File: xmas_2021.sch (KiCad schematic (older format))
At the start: 45 parts, among them J1 SWIM, Q1 MMBT3904, SW1 User, U1 STM8L101F2P3

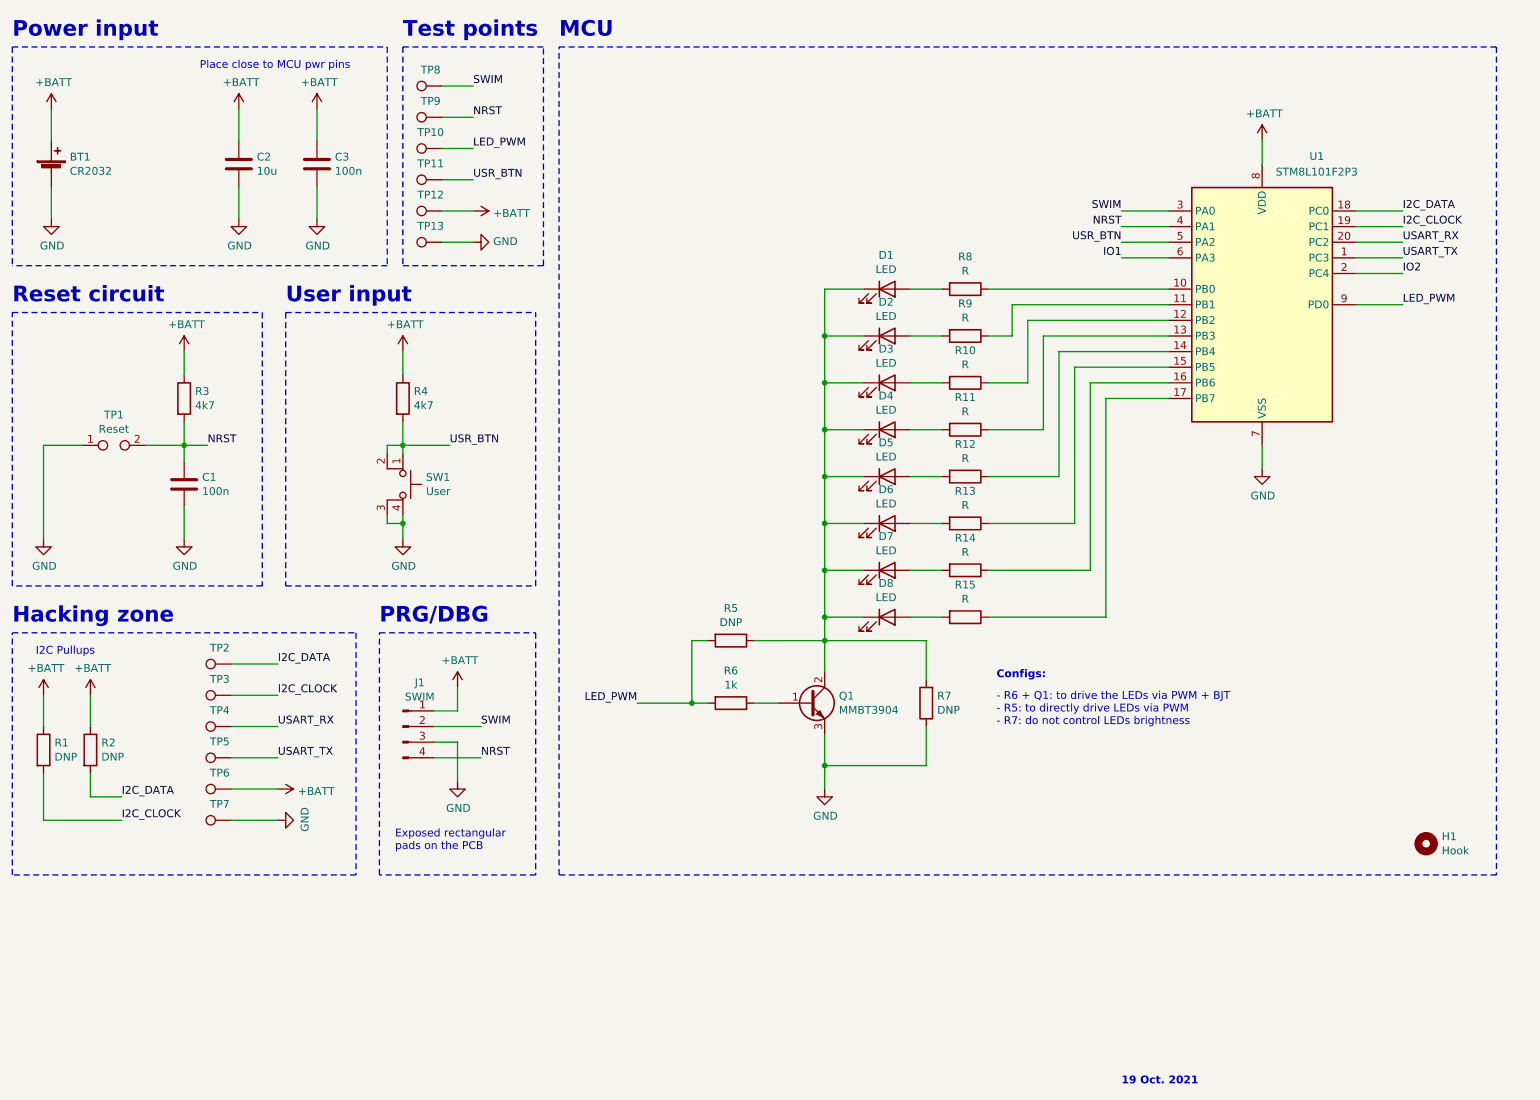
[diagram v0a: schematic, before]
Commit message: sch: update after hw test
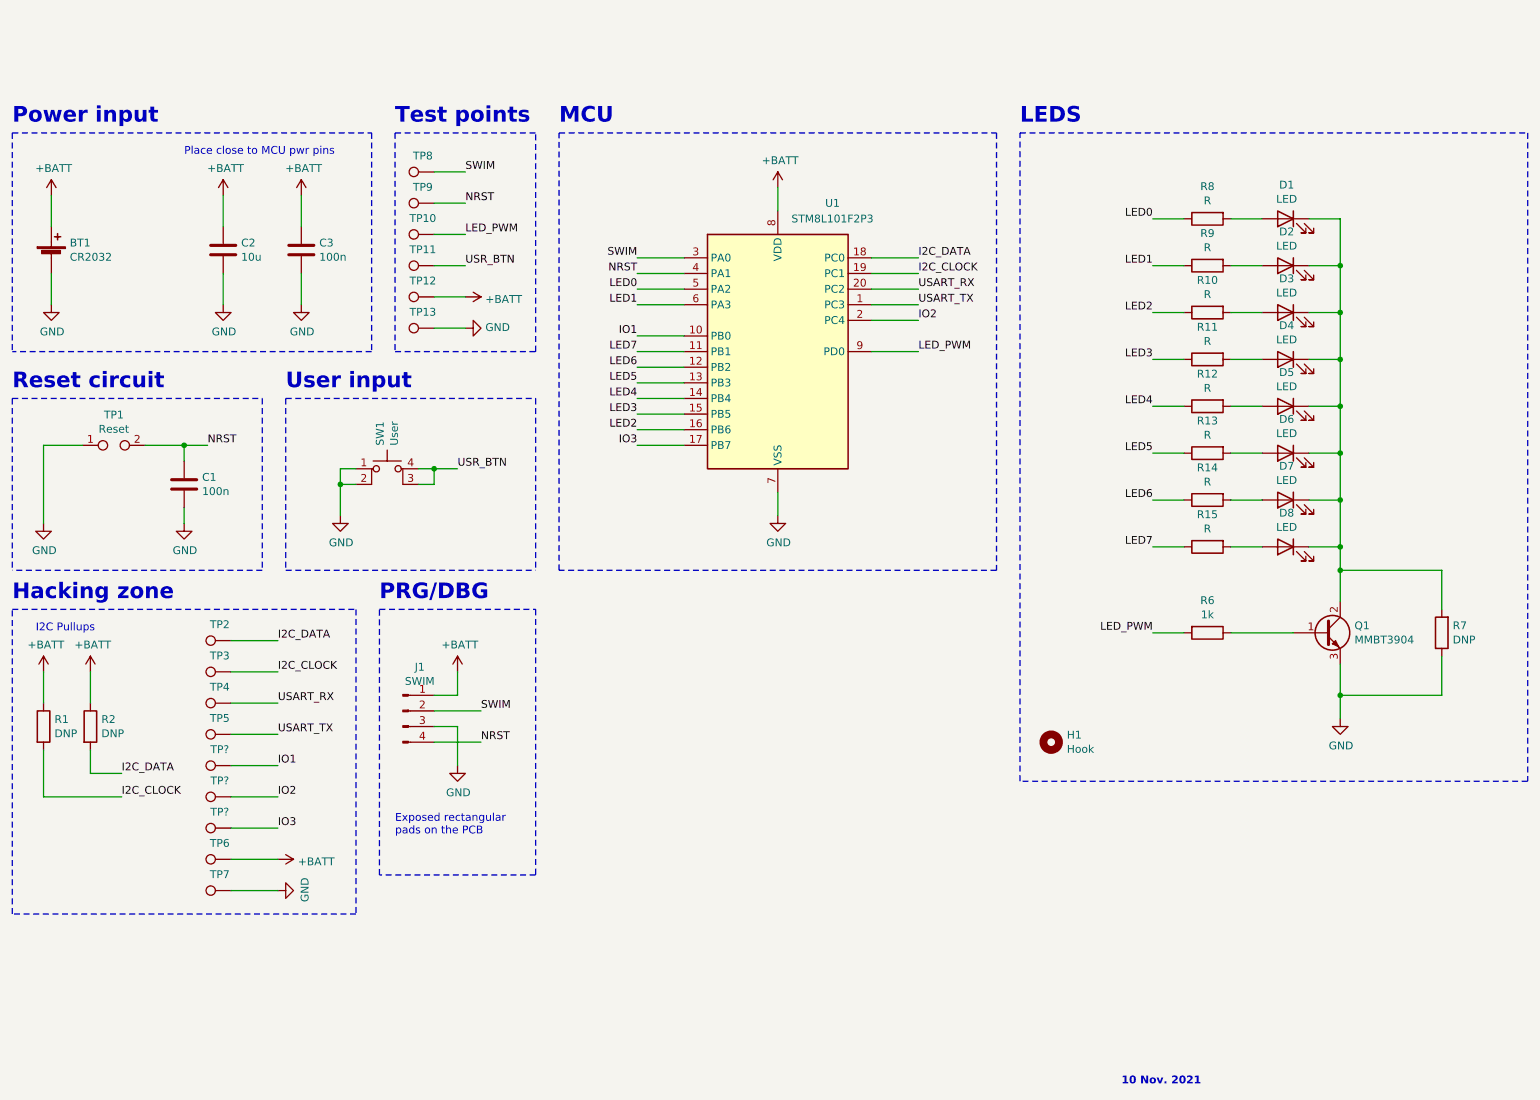
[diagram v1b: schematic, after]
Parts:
- removed R3, R4: 4k7, symbol Device:R
- removed R5: DNP, symbol Device:R
- added TP? (x3): USART_TX, symbol Connector:TestPoint
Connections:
- net GND: now also SW1.1, SW1.2; no longer SW1.3 (K), SW1.4 (A)
- net IO1: now also U1.10 (PB0), TP?.1; no longer U1.6 (PA3)
- net IO2: now also TP?.1
- net USR_BTN: now also SW1.3 (K), SW1.4 (A); no longer SW1.1, SW1.2, U1.5 (PA2)
- net LED0: now reaches R8.1
- net LED0: now also U1.5 (PA2); no longer U1.10 (PB0)
- net LED1: now reaches R9.1
- net LED1: now also U1.6 (PA3); no longer U1.11 (PB1)
- net LED2: now reaches R10.1
- net LED2: now also U1.16 (PB6); no longer U1.12 (PB2)
- net LED3: now reaches R11.1
- net LED3: now also U1.15 (PB5); no longer U1.13 (PB3)
- net LED4: now reaches R12.1, U1.14 (PB4)
- net LED5: now reaches R13.1
- net LED5: now also U1.13 (PB3); no longer U1.15 (PB5)
- net LED6: now reaches R14.1
- net LED6: now also U1.12 (PB2); no longer U1.16 (PB6)
- net IO3: now reaches U1.17 (PB7)
- net IO3: now also TP?.1; no longer R15.1
- new net LED7: R15.1, U1.11 (PB1)
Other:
- note added: "10 Nov. 2021"
- note added: "LEDS"
- note removed: "- R6 + Q1: to drive the LEDs via PWM + BJT\n- R5: to directly drive LEDs via PWM\n- R7: do not control LEDs brightness"
- note removed: "19 Oct. 2021"
- note removed: "Configs:"
- moved on the sheet: BT1, C2, C3, D1, D2, D3, D4, D5, D6, D7, D8, H1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

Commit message: first version
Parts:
- removed D8: LED, symbol Device:LED
- removed H1: Hook, symbol Mechanical:MountingHole
- removed Q1: MMBT3904, symbol Device:Q_NPN_BCE
- removed R15: R, symbol Device:R
- removed R6: 1k, symbol Device:R
- removed R7: DNP, symbol Device:R
- removed TP1: Reset, symbol Connector:TestPoint_2Pole
- removed TP10, TP6, TP7: USART_TX, symbol Connector:TestPoint
- BT1: footprint (none) -> xmas_2021:HLD-001
- C1, C2, C3: footprint (none) -> Capacitor_SMD:C_0603_1608Metric_Pad1.08x0.95mm_HandSolder
- D1, D2, D3, D4, D5, D6, D7: footprint (none) -> LED_SMD:LED_0603_1608Metric_Pad1.05x0.95mm_HandSolder
- J1: footprint (none) -> xmas_2021:swim
- R1, R2: footprint (none) -> Resistor_SMD:R_0603_1608Metric_Pad0.98x0.95mm_HandSolder
- R3: renamed from R8; footprint (none) -> Resistor_SMD:R_0603_1608Metric_Pad0.98x0.95mm_HandSolder
- R4: renamed from R9; footprint (none) -> Resistor_SMD:R_0603_1608Metric_Pad0.98x0.95mm_HandSolder
- R5: renamed from R10; footprint (none) -> Resistor_SMD:R_0603_1608Metric_Pad0.98x0.95mm_HandSolder
- R6: renamed from R11; footprint (none) -> Resistor_SMD:R_0603_1608Metric_Pad0.98x0.95mm_HandSolder
- R7: renamed from R12; footprint (none) -> Resistor_SMD:R_0603_1608Metric_Pad0.98x0.95mm_HandSolder
- R8: renamed from R13; footprint (none) -> Resistor_SMD:R_0603_1608Metric_Pad0.98x0.95mm_HandSolder
- R9: renamed from R14; footprint (none) -> Resistor_SMD:R_0603_1608Metric_Pad0.98x0.95mm_HandSolder
- SW1: footprint (none) -> xmas_2021:button
- TP10: renamed from TP8; value USART_TX -> SWIM; footprint (none) -> TestPoint:TestPoint_Pad_D1.0mm
- TP11: renamed from TP9; value USART_TX -> NRST; footprint (none) -> TestPoint:TestPoint_Pad_D1.0mm
- TP12: renamed from TP11; value USART_TX -> USR_BTN; footprint (none) -> TestPoint:TestPoint_Pad_D1.0mm
- TP13: renamed from TP12; value USART_TX -> VBATT; footprint (none) -> TestPoint:TestPoint_Pad_D1.0mm
- TP14: renamed from TP13; value USART_TX -> GND; footprint (none) -> TestPoint:TestPoint_Pad_D1.0mm
- TP2, TP3, TP4, TP5: footprint (none) -> TestPoint:TestPoint_Pad_D1.0mm
- TP6: renamed from TP?; value USART_TX -> IO1; footprint (none) -> TestPoint:TestPoint_Pad_D1.0mm
- TP7: renamed from TP?; value USART_TX -> IO2; footprint (none) -> TestPoint:TestPoint_Pad_D1.0mm
- TP8: renamed from TP?; value USART_TX -> IO3; footprint (none) -> TestPoint:TestPoint_Pad_D1.0mm
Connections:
- net LED7 is gone; now on net LED5: U1.11 (PB1)
- net LED_PWM is gone; now on net IO3: U1.9 (PD0)
- net GND: now also D1.1 (K), D2.1 (K), D3.1 (K), D4.1 (K), D5.1 (K), D6.1 (K), D7.1 (K)
- net IO1: now also U1.5 (PA2); no longer U1.10 (PB0)
- net IO3: no longer U1.17 (PB7)
- net LED0: now also U1.16 (PB6); no longer U1.5 (PA2)
- net LED1: now also U1.15 (PB5); no longer U1.6 (PA3)
- net LED2: now also U1.14 (PB4); no longer U1.16 (PB6)
- net LED3: now also U1.13 (PB3); no longer U1.15 (PB5)
- net LED4: now also U1.12 (PB2); no longer U1.14 (PB4)
- net LED5: no longer U1.13 (PB3)
- net LED6: now also U1.10 (PB0); no longer U1.12 (PB2)
- net USR_BTN: no longer names the net of SW1.4 (A), TP12.1
- net USR_BTN: no longer SW1.3 (K)
- new net: SW1.3 (K), U1.17 (PB7)
- no-connect marks 0 -> 1
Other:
- note added: "21 Nov. 2021"
- note removed: "10 Nov. 2021"
- note removed: "Reset circuit"
- note removed: "User input"
- moved on the sheet: BT1, C1, C2, C3, D1, D2, D3, D4, D5, D6, D7, J1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

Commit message: battery holder is now BH57A-5
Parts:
- BT1: footprint xmas_2021:HLD-001 -> xmas_2021:BH57A-5
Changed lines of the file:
@@
 F 0 "BT1" H 1618 3296 50  0000 L CNN
 F 1 "CR2032" H 1618 3205 50  0000 L CNN
-F 2 "xmas_2021:HLD-001" V 1500 3260 50  0001 C CNN
+F 2 "xmas_2021:BH57A-5" V 1500 3260 50  0001 C CNN
 F 3 "~" V 1500 3260 50  0001 C CNN
 	1    1500 3200

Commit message: minor fixes
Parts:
- BT1: value CR2032 -> CR1620
- R3, R4, R5, R6, R7, R8, R9: value R -> 150
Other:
- note added: "15 Dec. 2021"
- note removed: "21 Nov. 2021"
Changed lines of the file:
@@
 P 1500 3200
 F 0 "BT1" H 1618 3296 50  0000 L CNN
-F 1 "CR2032" H 1618 3205 50  0000 L CNN
+F 1 "CR1620" H 1618 3205 50  0000 L CNN
 F 2 "xmas_2021:BH57A-5" V 1500 3260 50  0001 C CNN
 F 3 "~" V 1500 3260 50  0001 C CNN
@@
 	8000 3850 7700 3850
 Text Notes 8150 7650 0    50   ~ 10
-21 Nov. 2021
+15 Dec. 2021
 Wire Wire Line
 	5050 4550 4950 4550
@@
 P 9400 4950
 F 0 "R9" V 9193 4950 50  0000 C CNN
-F 1 "R" V 9284 4950 50  0000 C CNN
+F 1 "150" V 9284 4950 50  0000 C CNN
 F 2 "Resistor_SMD:R_0603_1608Metric_Pad0.98x0.95mm_HandSolder" V 9330 4950 50  0001 C CNN
 F 3 "~" H 9400 4950 50  0001 C CNN
@@
 P 9400 4650
 F 0 "R8" V 9193 4650 50  0000 C CNN
-F 1 "R" V 9284 4650 50  0000 C CNN
+F 1 "150" V 9284 4650 50  0000 C CNN
 F 2 "Resistor_SMD:R_0603_1608Metric_Pad0.98x0.95mm_HandSolder" V 9330 4650 50  0001 C CNN
 F 3 "~" H 9400 4650 50  0001 C CNN
@@
 P 9400 4350
 F 0 "R7" V 9193 4350 50  0000 C CNN
-F 1 "R" V 9284 4350 50  0000 C CNN
+F 1 "150" V 9284 4350 50  0000 C CNN
 F 2 "Resistor_SMD:R_0603_1608Metric_Pad0.98x0.95mm_HandSolder" V 9330 4350 50  0001 C CNN
 F 3 "~" H 9400 4350 50  0001 C CNN
@@
 P 9400 4050
 F 0 "R6" V 9193 4050 50  0000 C CNN
-F 1 "R" V 9284 4050 50  0000 C CNN
+F 1 "150" V 9284 4050 50  0000 C CNN
 F 2 "Resistor_SMD:R_0603_1608Metric_Pad0.98x0.95mm_HandSolder" V 9330 4050 50  0001 C CNN
 F 3 "~" H 9400 4050 50  0001 C CNN
@@
 P 9400 3450
 F 0 "R4" V 9193 3450 50  0000 C CNN
-F 1 "R" V 9284 3450 50  0000 C CNN
+F 1 "150" V 9284 3450 50  0000 C CNN
 F 2 "Resistor_SMD:R_0603_1608Metric_Pad0.98x0.95mm_HandSolder" V 9330 3450 50  0001 C CNN
 F 3 "~" H 9400 3450 50  0001 C CNN
@@
 P 9400 3750
 F 0 "R5" V 9193 3750 50  0000 C CNN
-F 1 "R" V 9284 3750 50  0000 C CNN
+F 1 "150" V 9284 3750 50  0000 C CNN
 F 2 "Resistor_SMD:R_0603_1608Metric_Pad0.98x0.95mm_HandSolder" V 9330 3750 50  0001 C CNN
 F 3 "~" H 9400 3750 50  0001 C CNN
@@
 P 9400 3150
 F 0 "R3" V 9193 3150 50  0000 C CNN
-F 1 "R" V 9284 3150 50  0000 C CNN
+F 1 "150" V 9284 3150 50  0000 C CNN
 F 2 "Resistor_SMD:R_0603_1608Metric_Pad0.98x0.95mm_HandSolder" V 9330 3150 50  0001 C CNN
 F 3 "~" H 9400 3150 50  0001 C CNN
